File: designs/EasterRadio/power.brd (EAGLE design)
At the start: 160 x 100 mm, 13 parts, among them IC1 MCP73832T-2ACI_OT, IC3 DMP1045U-7, J4 S2B-PH-SM4, J6 PJ-002AH-SMT-TR

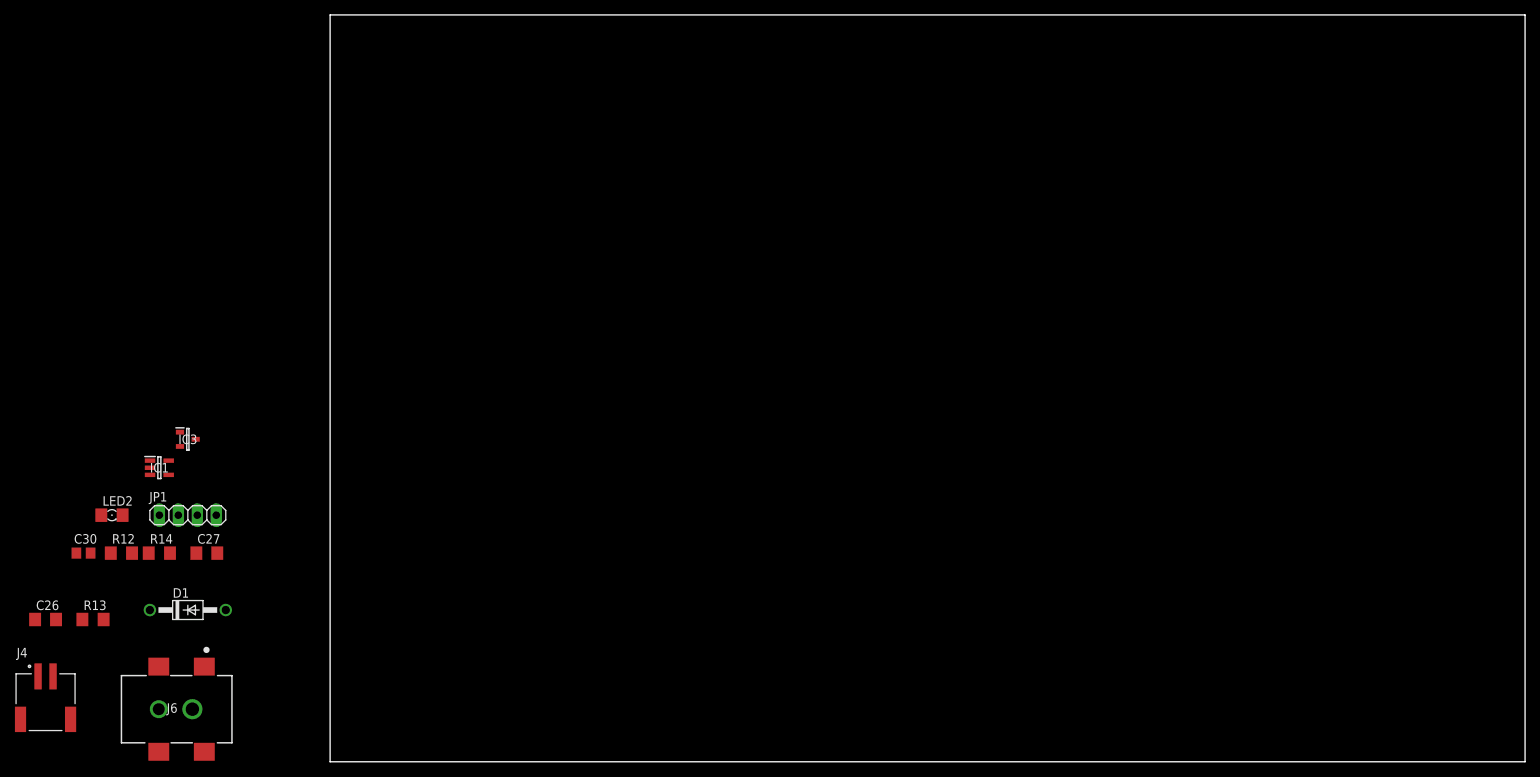
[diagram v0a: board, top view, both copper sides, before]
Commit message: changed to correct diode and designed power pcb
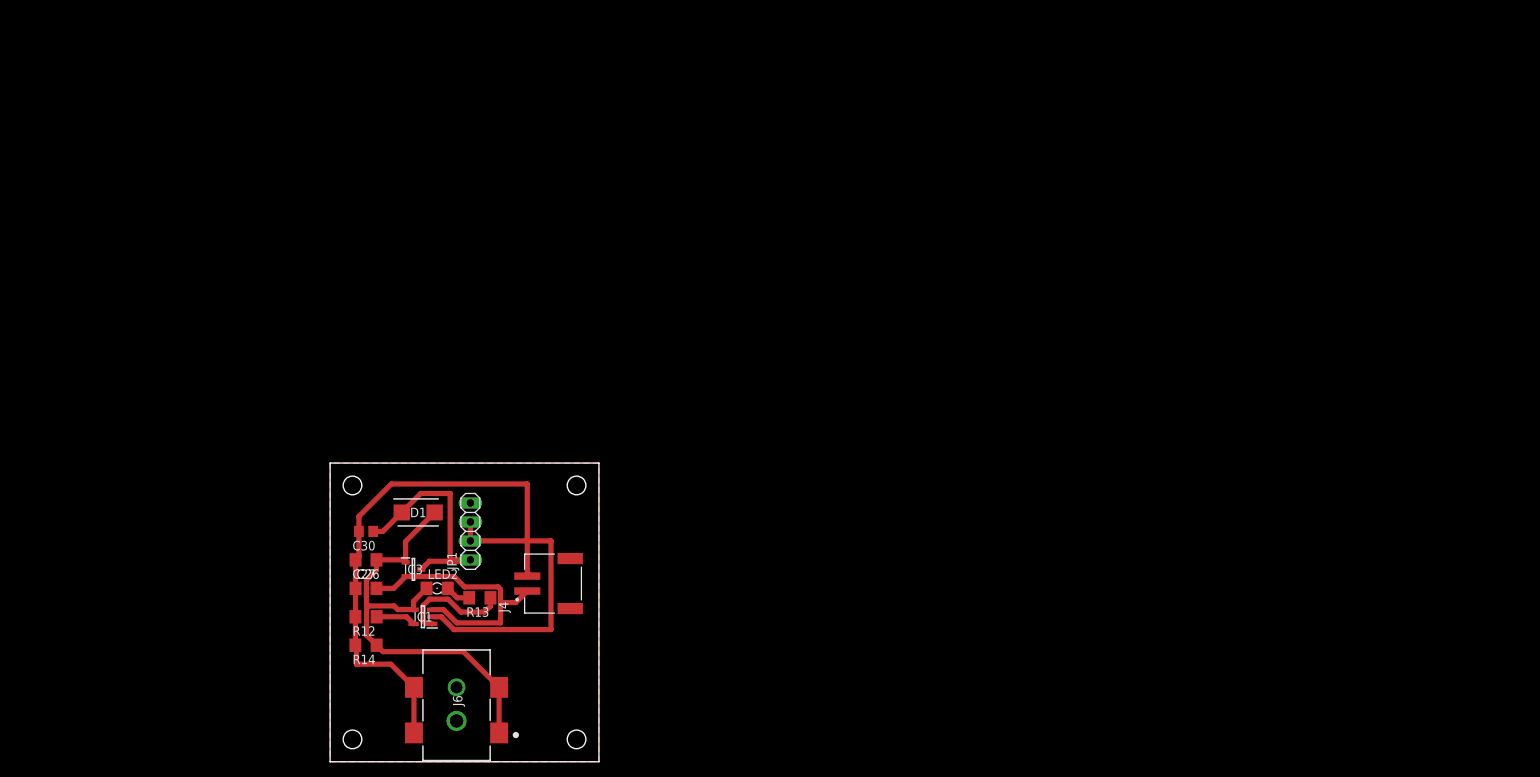
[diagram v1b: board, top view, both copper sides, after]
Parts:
- D1: value 1N4942 -> LSM115JE3_TR13; device diode:DO41-10 -> CommonParts:DIOM5436X330N
- moved J4 65.7 mm to (26.4, 23.9), turned to 90 degrees
- moved R13 51.9 mm to (20.1, 22.0), turned to 180 degrees
- moved LED2 44.6 mm to (14.3, 23.2)
- moved C26 43.1 mm to (4.81, 23.2)
- moved J6 42.2 mm to (12.4, 15.0), turned to 270 degrees
- moved IC1 40.5 mm to (12.4, 19.4), turned to 180 degrees
- moved C30 37.9 mm to (4.81, 30.8), turned to 180 degrees
- moved JP1 37.9 mm to (18.8, 30.8), turned to 90 degrees
- moved IC3 34.9 mm to (11.2, 25.8)
- moved R12 33.8 mm to (4.81, 19.4), turned to 180 degrees
- moved D1 33.5 mm to (11.8, 33.4)
- moved R14 30.3 mm to (4.81, 15.6), turned to 180 degrees
- moved C27 21.3 mm to (4.81, 27.0), turned to 180 degrees
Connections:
- removed net 12V: C30.1, D1.C, IC3.3, J6.1, J6.2, JP1.1
- new net U_DRAIN: C30.1, D1.1, IC3.3, JP1.1
- net 5V: now also D1.2, J6.1, J6.2; no longer D1.A
- net GNDA: no longer J4.S1, J4.S2
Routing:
- net GNDA: track 0.00 -> 114.6 mm
- net 5V: track 0.00 -> 59.9 mm
- net VBAT: track 0.00 -> 36.6 mm
- net U_DRAIN: track 0.00 -> 31.1 mm
- net STAT: track 0.00 -> 15.0 mm
- net PROG: track 0.00 -> 5.34 mm
- net N$10: track 0.00 -> 3.40 mm
- added copper zone on layer 1, net GNDA
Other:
- board size 160 x 100 mm -> 36 x 40 mm
